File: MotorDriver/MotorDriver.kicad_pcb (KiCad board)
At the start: 2 copper layers, 25.4 x 23.9 mm, 21 parts, among them P1 CONN_01X04, P2 CONN_01X03, P4 CONN_01X02, U1 TB6593FNG

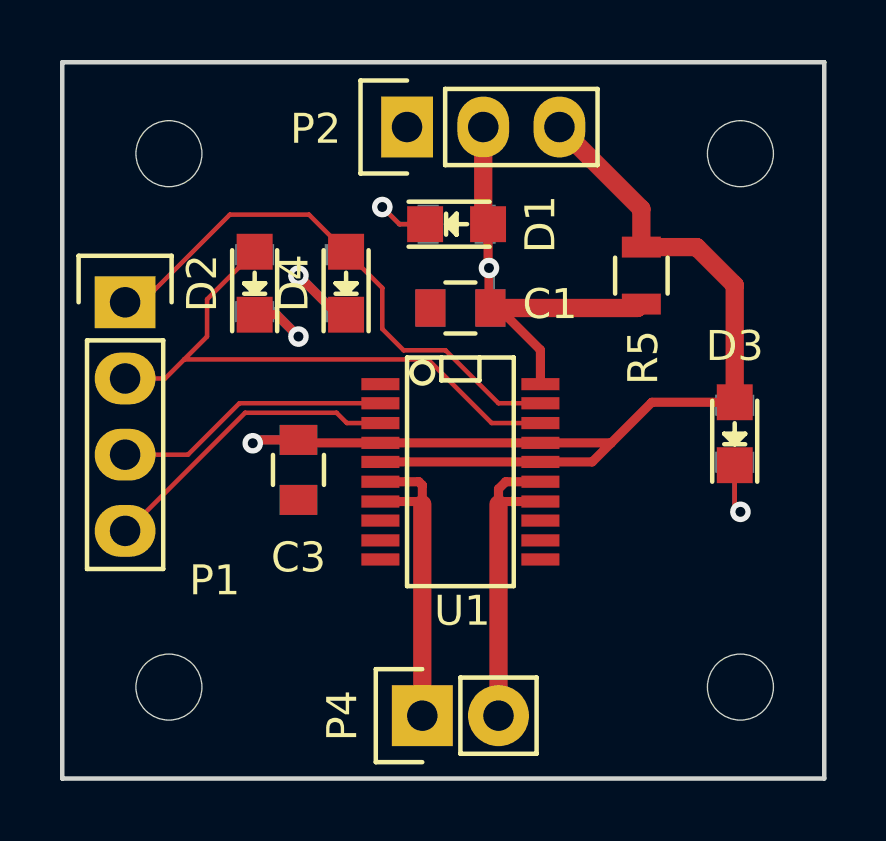
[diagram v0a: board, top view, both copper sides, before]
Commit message: finished motor driver layout and generated gerbers
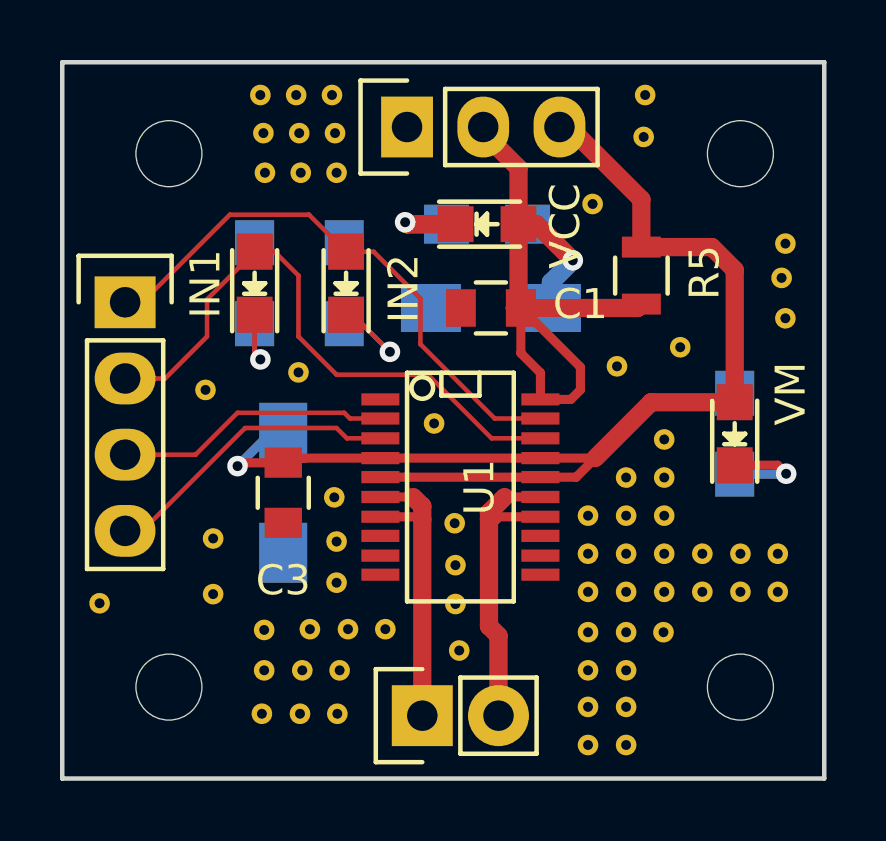
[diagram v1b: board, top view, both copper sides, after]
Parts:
- added REF**13: via, MotorDriver:via, F.Cu at (146.1, 98.4)
- added REF**14: via, MotorDriver:via, F.Cu at (146.2, 88.0)
- added REF**14: via, MotorDriver:via, F.Cu at (136.5, 87.0)
- added REF**14: via, MotorDriver:via, F.Cu at (136.4, 93.6)
- added REF**14: via, MotorDriver:via, F.Cu at (140.9, 95.4)
- added REF**14: via, MotorDriver:via, F.Cu at (135.2, 105.0)
- added REF**14: via, MotorDriver:via, F.Cu at (133.3, 94.2)
- added REF**14: via, MotorDriver:via, F.Cu at (135.3, 102.2)
- added REF**14: via, MotorDriver:via, F.Cu at (135.3, 103.6)
- added REF**14: via, MotorDriver:via, F.Cu at (136.8, 102.2)
- added REF**14: via, MotorDriver:via, F.Cu at (141.6, 101.4)
- added REF**14: via, MotorDriver:via, F.Cu at (146.1, 104.8)
- added REF**14: via, MotorDriver:via, F.Cu at (137.5, 84.4)
- added REF**14: via, MotorDriver:via, F.Cu at (146.1, 102.3)
- added REF**14: via, MotorDriver:via, F.Cu at (146.1, 99.7)
- added REF**14: via, MotorDriver:via, F.Cu at (135.1, 84.4)
- added REF**14: via, MotorDriver:via, F.Cu at (136.3, 84.4)
- added REF**14: via, MotorDriver:via, F.Cu at (136.4, 85.7)
- added REF**14: via, MotorDriver:via, F.Cu at (135.2, 85.7)
- added REF**14: via, MotorDriver:via, F.Cu at (137.6, 85.7)
- added REF**14: via, MotorDriver:via, F.Cu at (137.7, 87.0)
- added REF**14: via, MotorDriver:via, F.Cu at (135.3, 87.0)
- added REF**15: via, MotorDriver:via, F.Cu at (146.1, 106.1)
- added REF**15: via, MotorDriver:via, F.Cu at (146.1, 103.6)
- added REF**15: via, MotorDriver:via, F.Cu at (146.1, 101.0)
- added REF**22: via, MotorDriver:via, F.Cu at (147.3, 97.2)
- added REF**23: via, MotorDriver:via, F.Cu at (147.3, 98.4)
- added REF**24: via, MotorDriver:via, F.Cu at (136.4, 105.0)
- added REF**24: via, MotorDriver:via, F.Cu at (136.5, 103.6)
- added REF**24: via, MotorDriver:via, F.Cu at (141.6, 98.7)
- added REF**24: via, MotorDriver:via, F.Cu at (138.0, 102.2)
- added REF**24: via, MotorDriver:via, F.Cu at (139.3, 102.2)
- added REF**24: via, MotorDriver:via, F.Cu at (141.8, 102.9)
- added REF**24: via, MotorDriver:via, F.Cu at (141.6, 100.1)
- added REF**24: via, MotorDriver:via, F.Cu at (148.6, 102.3)
- added REF**24: via, MotorDriver:via, F.Cu at (147.3, 104.8)
- added REF**24: via, MotorDriver:via, F.Cu at (147.3, 102.3)
- added REF**24: via, MotorDriver:via, F.Cu at (147.3, 99.7)
- added REF**24: via, MotorDriver:via, F.Cu at (137.7, 105.0)
- added REF**24: via, MotorDriver:via, F.Cu at (129.8, 101.3)
- added REF**24: via, MotorDriver:via, F.Cu at (133.6, 99.2)
- added REF**24: via, MotorDriver:via, F.Cu at (133.6, 101.0)
- added REF**24: via, MotorDriver:via, F.Cu at (137.6, 97.8)
- added REF**24: via, MotorDriver:via, F.Cu at (137.7, 99.3)
- added REF**24: via, MotorDriver:via, F.Cu at (137.7, 100.7)
- added REF**24: via, MotorDriver:via, F.Cu at (137.8, 103.6)
- added REF**25: via, MotorDriver:via, F.Cu at (147.3, 106.1)
- added REF**25: via, MotorDriver:via, F.Cu at (147.3, 103.6)
- added REF**25: via, MotorDriver:via, F.Cu at (147.3, 101.0)
- added REF**31: via, MotorDriver:via, F.Cu at (148.6, 95.9)
- added REF**32: via, MotorDriver:via, F.Cu at (148.6, 97.2)
- added REF**33: via, MotorDriver:via, F.Cu at (148.6, 98.4)
- added REF**34: via, MotorDriver:via, F.Cu at (148.6, 99.7)
- added REF**35: via, MotorDriver:via, F.Cu at (148.6, 101.0)
- added REF**44: via, MotorDriver:via, F.Cu at (147.0, 93.4)
- added REF**44: via, MotorDriver:via, F.Cu at (149.1, 92.8)
- added REF**44: via, MotorDriver:via, F.Cu at (147.9, 85.8)
- added REF**44: via, MotorDriver:via, F.Cu at (148.0, 84.4)
- added REF**44: via, MotorDriver:via, F.Cu at (152.6, 89.4)
- added REF**44: via, MotorDriver:via, F.Cu at (152.5, 90.5)
- added REF**44: via, MotorDriver:via, F.Cu at (152.6, 91.8)
- added REF**44: via, MotorDriver:via, F.Cu at (149.9, 99.7)
- added REF**45: via, MotorDriver:via, F.Cu at (149.9, 101.0)
- added REF**54: via, MotorDriver:via, F.Cu at (152.4, 101.0)
- added REF**54: via, MotorDriver:via, F.Cu at (152.4, 99.7)
- added REF**54: via, MotorDriver:via, F.Cu at (151.1, 99.7)
- added REF**55: via, MotorDriver:via, F.Cu at (151.1, 101.0)
- C2, C4: footprint Capacitors_SMD:C_0805 -> Capacitors_SMD:C_1206_HandSoldering
- R1, R2, R3, R4: footprint Resistors_SMD:R_0805 -> Resistors_SMD:R_0805_HandSoldering
- moved D1 1.02 mm to (142.7, 88.7)
- moved R1 1.02 mm to (142.7, 88.7)
- moved C1 1.02 mm to (142.8, 91.5)
- moved C2 1.02 mm to (142.8, 91.5)
- moved C3 0.92 mm to (135.9, 97.7)
- moved C4 0.92 mm to (135.9, 97.7)
- moved U1 0.51 mm to (141.8, 97.5)
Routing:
- net VCC: track 16.6 -> 23.5 mm
- net /VM: track 38.9 -> 40.0 mm
- net Net-(D2-Pad1): track 3.57 -> 2.84 mm
- net /IN1: track 19.5 -> 20.1 mm
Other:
- rule pad_to_mask_clearance: 0.2 -> 0.0508
- board text added: "GND"
- board text added: "GoGoGo Alan Ford"
- board text added: "IN1"
- board text added: "IN2"
- board text added: "O1"
- board text added: "O2"
- board text added: "PWM"
- board text added: "STBY"
- board text added: "VCC"
- board text added: "VM"
